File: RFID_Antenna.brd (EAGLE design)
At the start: 25.4 x 38.1 mm, 26 parts, among them J1 U.FL

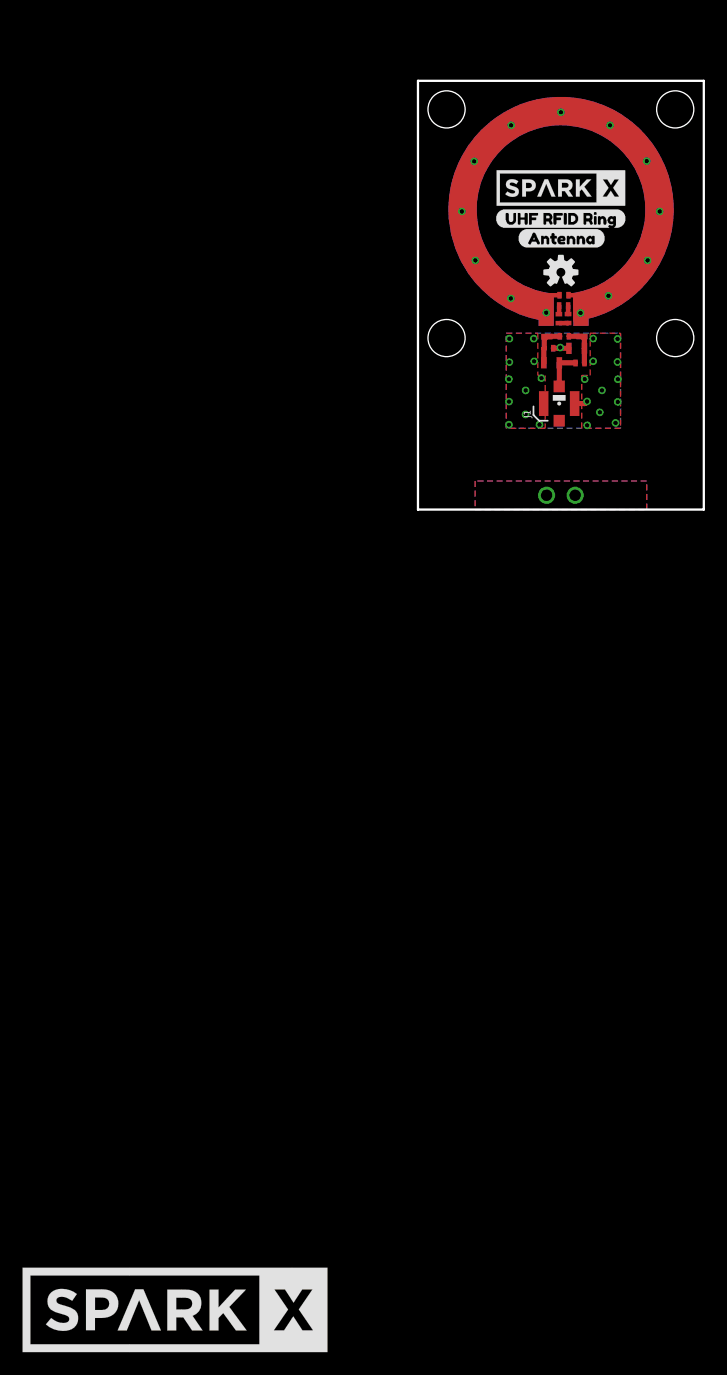
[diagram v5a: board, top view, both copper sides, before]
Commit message: Linked SparkX logo between schematic and brd
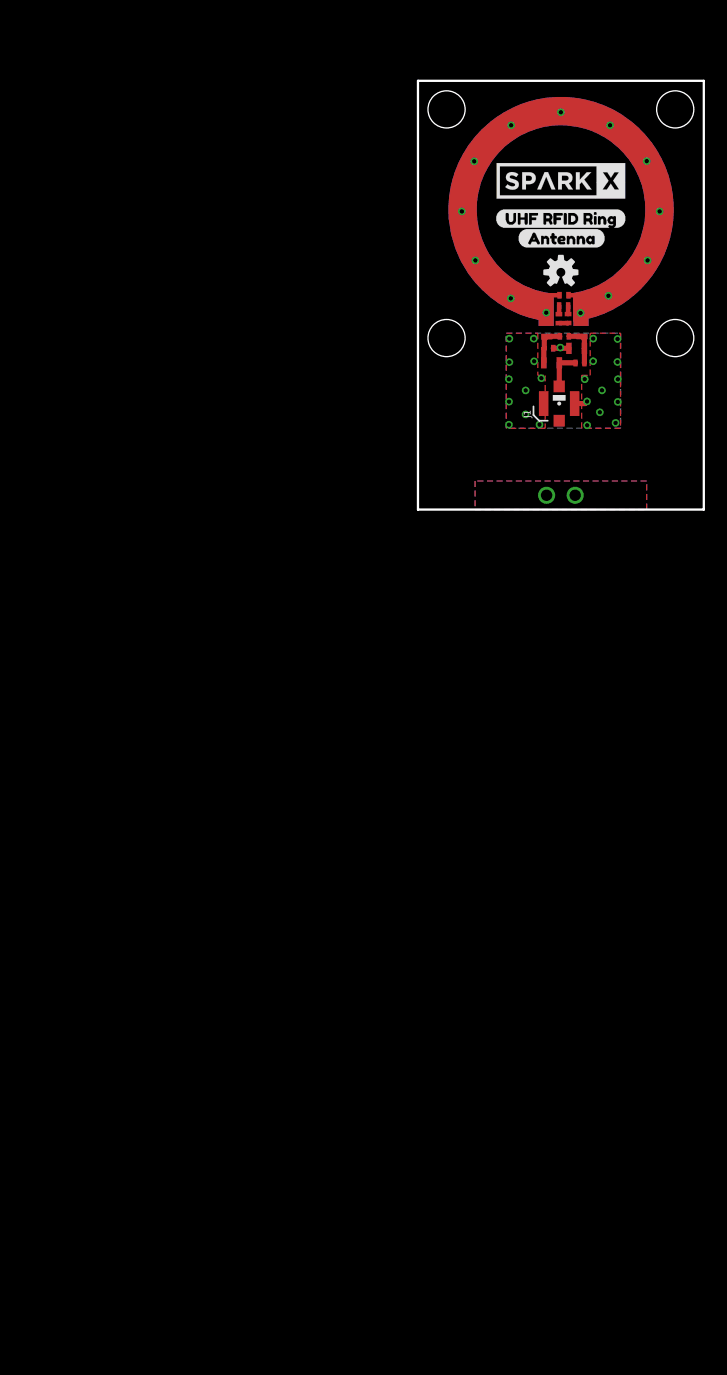
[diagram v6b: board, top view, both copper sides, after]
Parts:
- removed U$3: (no value), SparkX:SPARKX-LARGE
- U$12: value SPARKX-LOGO6 -> SPARKX-LOGO5; device SparkX:SPARKX-XLARGE -> SparkX:SPARKX-LARGE
- moved U$12 106.0 mm to (12.7, 29.2)
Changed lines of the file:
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@@
 <grid distance="0.05" unitdist="inch" unit="inch" style="lines" multiple="1" display="yes" altdistance="0.005" altunitdist="inch" altunit="inch"/>
 <layers>
-<layer number="1" name="Top" color="4" fill="1" visible="yes" active="yes"/>
-<layer number="16" name="Bottom" color="1" fill="1" visible="yes" active="yes"/>
+<layer number="1" name="Top" color="4" fill="1" visible="no" active="yes"/>
+<layer number="16" name="Bottom" color="1" fill="1" visible="no" active="yes"/>
 <layer number="17" name="Pads" color="2" fill="1" visible="yes" active="yes"/>
-<layer number="18" name="Vias" color="2" fill="1" visible="yes" active="yes"/>
-<layer number="19" name="Unrouted" color="6" fill="1" visible="yes" active="yes"/>
+<layer number="18" name="Vias" color="2" fill="1" visible="no" active="yes"/>
+<layer number="19" name="Unrouted" color="6" fill="1" visible="no" active="yes"/>
 <layer number="20" name="Dimension" color="15" fill="1" visible="yes" active="yes"/>
 <layer number="21" name="tPlace" color="16" fill="1" visible="yes" active="yes"/>
-<layer number="22" name="bPlace" color="14" fill="1" visible="yes" active="yes"/>
+<layer number="22" name="bPlace" color="14" fill="1" visible="no" active="yes"/>
 <layer number="23" name="tOrigins" color="15" fill="1" visible="yes" active="yes"/>
-<layer number="24" name="bOrigins" color="15" fill="1" visible="yes" active="yes"/>
-<layer number="25" name="tNames" color="7" fill="1" visible="yes" active="yes"/>
-<layer number="26" name="bNames" color="7" fill="1" visible="yes" active="yes"/>
+<layer number="24" name="bOrigins" color="15" fill="1" visible="no" active="yes"/>
+<layer number="25" name="tNames" color="7" fill="1" visible="no" active="yes"/>
+<layer number="26" name="bNames" color="7" fill="1" visible="no" active="yes"/>
 <layer number="27" name="tValues" color="7" fill="1" visible="yes" active="yes"/>
-<layer number="28" name="bValues" color="7" fill="1" visible="yes" active="yes"/>
-<layer number="29" name="tStop" color="7" fill="3" visible="yes" active="yes"/>
-<layer number="30" name="bStop" color="7" fill="6" visible="yes" active="yes"/>
+<layer number="28" name="bValues" color="7" fill="1" visible="no" active="yes"/>
+<layer number="29" name="tStop" color="7" fill="3" visible="no" active="yes"/>
+<layer number="30" name="bStop" color="7" fill="6" visible="no" active="yes"/>
 <layer number="31" name="tCream" color="7" fill="4" visible="yes" active="yes"/>
-<layer number="32" name="bCream" color="7" fill="5" visible="yes" active="yes"/>
-<layer number="33" name="tFinish" color="6" fill="3" visible="yes" active="yes"/>
-<layer number="34" name="bFinish" color="6" fill="6" visible="yes" active="yes"/>
-<layer number="35" name="tGlue" color="7" fill="4" visible="yes" active="yes"/>
-<layer number="36" name="bGlue" color="7" fill="5" visible="yes" active="yes"/>
-<layer number="37" name="tTest" color="7" fill="1" visible="yes" active="yes"/>
-<layer number="38" name="bTest" color="7" fill="1" visible="yes" active="yes"/>
-<layer number="39" name="tKeepout" color="4" fill="11" visible="yes" active="yes"/>
-<layer number="40" name="bKeepout" color="1" fill="11" visible="yes" active="yes"/>
-<layer number="41" name="tRestrict" color="4" fill="10" visible="yes" active="yes"/>
-<layer number="42" name="bRestrict" color="1" fill="10" visible="yes" active="yes"/>
-<layer number="43" name="vRestrict" color="2" fill="10" visible="yes" active="yes"/>
-<layer number="44" name="Drills" color="7" fill="1" visible="yes" active="yes"/>
+<layer number="32" name="bCream" color="7" fill="5" visible="no" active="yes"/>
+<layer number="33" name="tFinish" color="6" fill="3" visible="no" active="yes"/>
+<layer number="34" name="bFinish" color="6" fill="6" visible="no" active="yes"/>
+<layer number="35" name="tGlue" color="7" fill="4" visible="no" active="yes"/>
+<layer number="36" name="bGlue" color="7" fill="5" visible="no" active="yes"/>
+<layer number="37" name="tTest" color="7" fill="1" visible="no" active="yes"/>
+<layer number="38" name="bTest" color="7" fill="1" visible="no" active="yes"/>
+<layer number="39" name="tKeepout" color="4" fill="11" visible="no" active="yes"/>
+<layer number="40" name="bKeepout" color="1" fill="11" visible="no" active="yes"/>
+<layer number="41" name="tRestrict" color="4" fill="10" visible="no" active="yes"/>
+<layer number="42" name="bRestrict" color="1" fill="10" visible="no" active="yes"/>
+<layer number="43" name="vRestrict" color="2" fill="10" visible="no" active="yes"/>
+<layer number="44" name="Drills" color="7" fill="1" visible="no" active="yes"/>
 <layer number="45" name="Holes" color="7" fill="1" visible="yes" active="yes"/>
-<layer number="46" name="Milling" color="3" fill="1" visible="yes" active="yes"/>
-<layer number="47" name="Measures" color="7" fill="1" visible="yes" active="yes"/>
-<layer number="48" name="Document" color="7" fill="1" visible="yes" active="yes"/>
-<layer number="49" name="Reference" color="7" fill="1" visible="yes" active="yes"/>
-<layer number="50" name="dxf" color="7" fill="1" visible="yes" active="yes"/>
+<layer number="46" name="Milling" color="3" fill="1" visible="no" active="yes"/>
+<layer number="47" name="Measures" color="7" fill="1" visible="no" active="yes"/>
+<layer number="48" name="Document" color="7" fill="1" visible="no" active="yes"/>
+<layer number="49" name="Reference" color="7" fill="1" visible="no" active="yes"/>
+<layer number="50" name="dxf" color="7" fill="1" visible="no" active="yes"/>
 <layer number="51" name="tDocu" color="6" fill="1" visible="yes" active="yes"/>
-<layer number="52" name="bDocu" color="7" fill="1" visible="yes" active="yes"/>
+<layer number="52" name="bDocu" color="7" fill="1" visible="no" active="yes"/>
 <layer number="91" name="Nets" color="2" fill="1" visible="no" active="no"/>
 <layer number="92" name="Busses" color="1" fill="1" visible="no" active="no"/>
@@
 </element>
 <element name="C5" library="SparkFun-Capacitors" package="0402_MURATA" value="2.4 pF" x="11.6212" y="14.3352" smashed="yes" rot="R180">
-<attribute name="PROD_ID" value="CAP-14351" x="11.6212" y="14.3352" size="1.778" layer="27" rot="R180" display="off"/>
+<attribute name="PROD_ID" value="14351" x="11.6212" y="14.3352" size="1.778" layer="27" rot="R180" display="off"/>
 <attribute name="VALUE" value="2.4 pF" x="11.6212" y="14.3352" size="1.778" layer="27" rot="R180" display="off"/>
 </element>
 <element name="C6" library="SparkFun-Capacitors" package="0402_MURATA" value="2.4 pF" x="14.3952" y="13.0242" smashed="yes" rot="R180">
-<attribute name="PROD_ID" value="CAP-14351" x="14.3952" y="13.0242" size="1.778" layer="27" rot="R180" display="off"/>
+<attribute name="PROD_ID" value="14351" x="14.3952" y="13.0242" size="1.778" layer="27" rot="R180" display="off"/>
 <attribute name="VALUE" value="2.4 pF" x="14.3952" y="13.0242" size="1.778" layer="27" rot="R180" display="off"/>
 </element>
@@
 <element name="U$1" library="special_parts" package="ANT" value="ANTENNA" x="12.7112" y="26.6632" smashed="yes"/>
 <element name="U$2" library="SparkFun-Aesthetics" package="ORDERING_INSTRUCTIONS" value="SPECIAL_INSTRUCTIONS-ORDERING" x="-34.29" y="-5.08" smashed="yes"/>
-<element name="U$3" library="SparkX" package="SPARKX-LARGE" value="" x="12.7" y="28.575" smashed="yes"/>
 <element name="U$4" library="SparkX" package="SPARKX-LARGE" value="" x="12.7" y="28.575" smashed="yes" rot="MR0"/>
 <element name="U$5" library="buzzard_labels" package="UHF_RFID_RING0" value="" x="6.8326" y="25.8572" smashed="yes"/>
@@
 <element name="U$10" library="SparkFun-Aesthetics" package="OSHW-LOGO-S" value="" x="12.7" y="21.082" smashed="yes"/>
 <element name="U$11" library="SparkX" package="QWIIC_BOARD_MOUNT_HOLES" value="" x="12.7" y="25.4" smashed="yes" rot="MR0"/>
-<element name="U$12" library="SparkX" package="SPARKX-XLARGE" value="SPARKX-LOGO6" x="-21.59" y="-71.12" smashed="yes"/>
+<element name="U$12" library="SparkX" package="SPARKX-LARGE" value="SPARKX-LOGO5" x="12.7" y="29.21" smashed="yes"/>
 </elements>
 <signals>
